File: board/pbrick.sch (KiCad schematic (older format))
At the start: 53 parts, among them J1 S8B-PH-SM4-TB_LF__SN_, J2 UJC-HP-3-SMT-TR, J3 QWIIC, J5 U.FL2PIN, J6 TC2030-IDC-NL, Q1 SSM6J507NU, Q2 SSM6J507NU, U1 TB67H420FTG(O,EL), U2 MIC5219-3.3YML-TR, U3 ADP3330ARTZ-5-RL7, U4 STUSB4500QTR

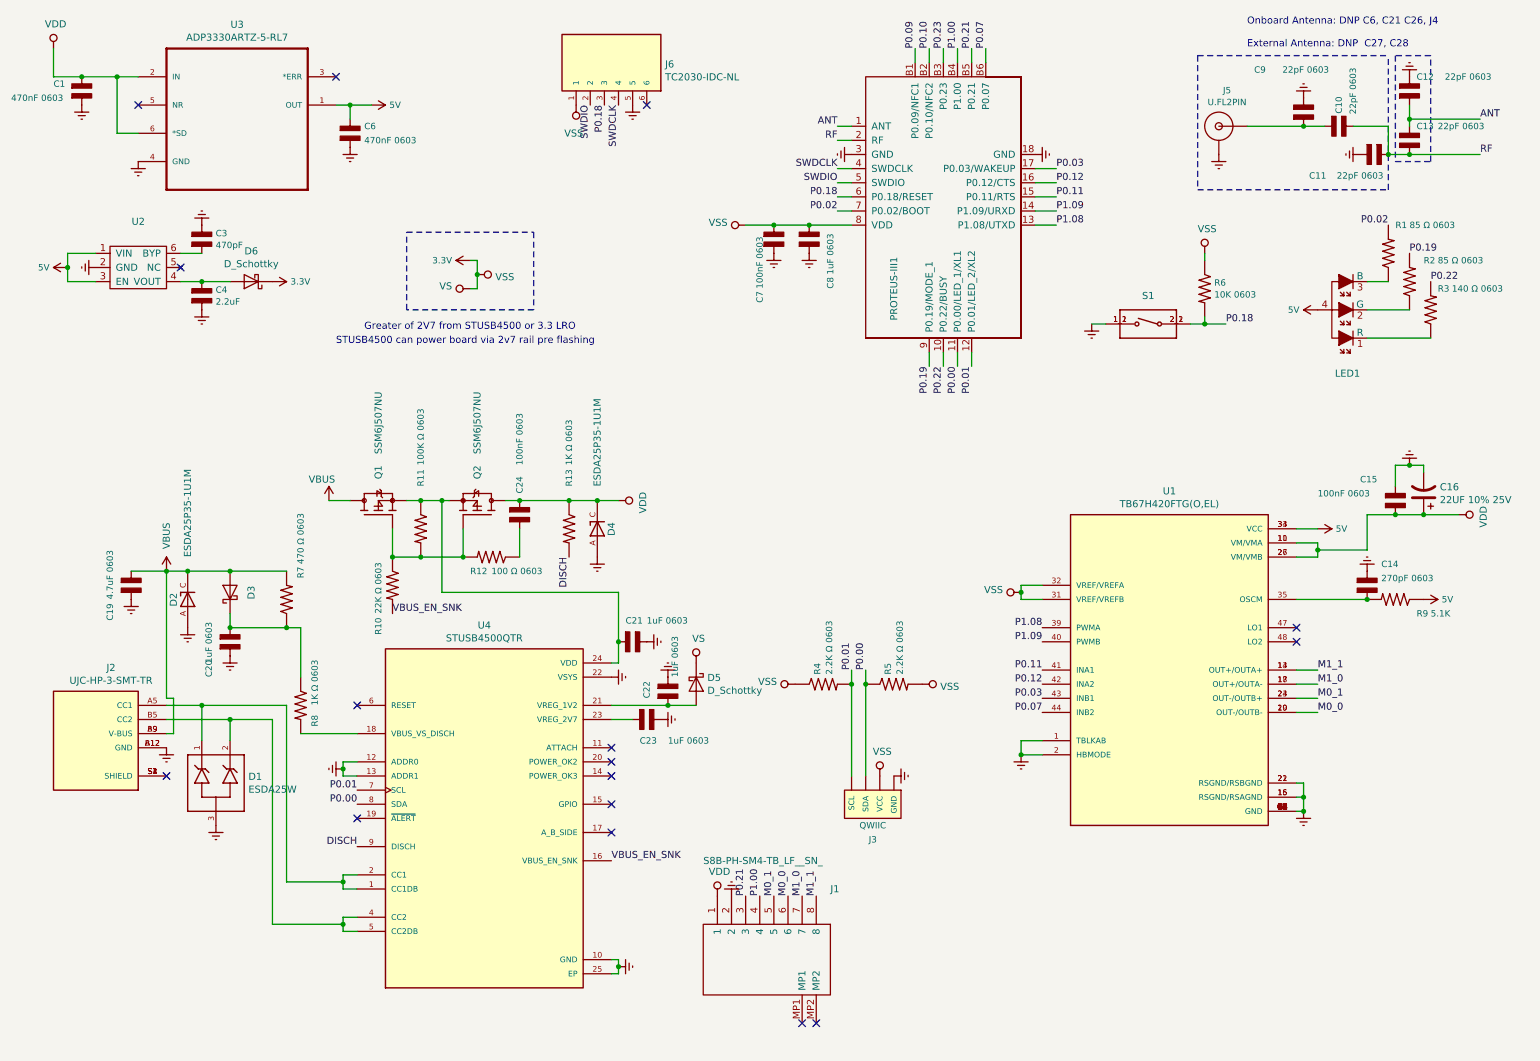
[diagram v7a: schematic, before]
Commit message: Starting work on STUSB4500 USB i2C connection for new board design
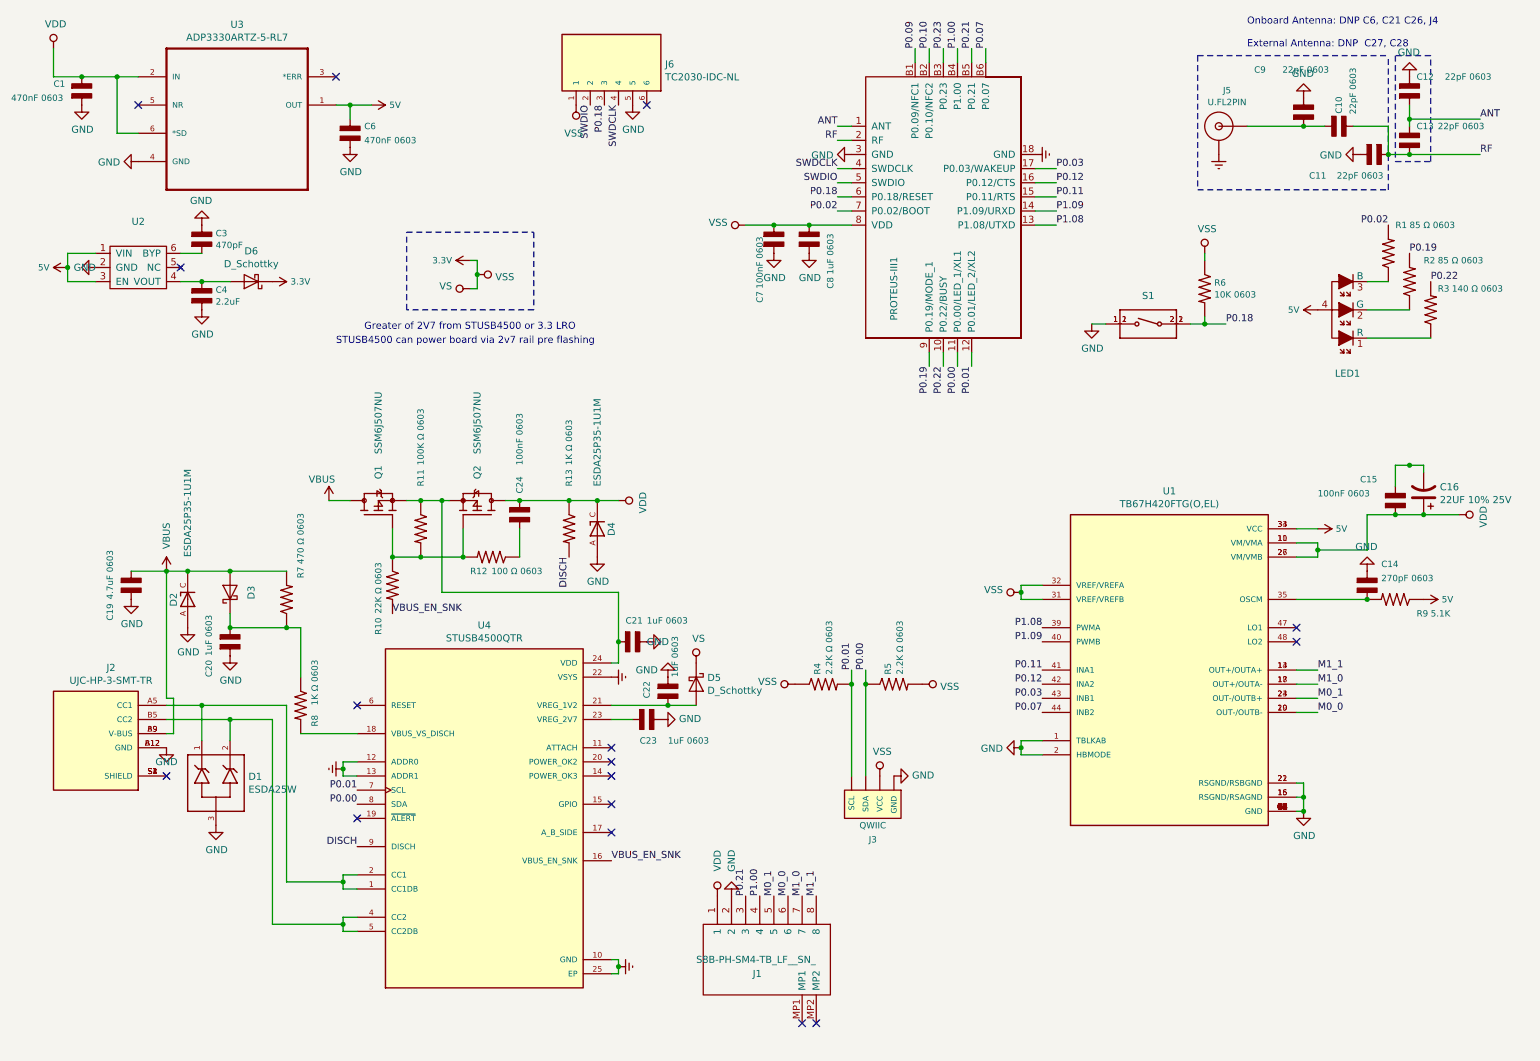
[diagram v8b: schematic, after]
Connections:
- net Earth: no longer C1.2, C11.2, C12.1, C14.1, C15.1, C16.2, C19.2, C20.2, C21.1, C22.1, C23.1, C3.1, C4.2, C6.2, C7.2, C8.2, C9.1, D1.3, D2.A, D4.A, J1.2, J2.A12 (GND), J2.B12 (GND), J3.1 (GND), J6.5, PROTEUS-III1.3 (GND), S1.1_1 (1), S1.1_2 (1), U1.1 (TBLKAB), U1.15 (RSGND/RSAGND), U1.16 (RSGND/RSAGND), U1.2 (HBMODE), U1.21 (RSGND/RSBGND), U1.22 (RSGND/RSBGND), U1.29 (GND), U1.30 (GND), U1.49 (GND), U1.50 (GND), U1.51 (GND), U1.52 (GND), U1.53 (GND), U1.54 (GND), U1.55 (GND), U1.56 (GND), U1.57 (GND), U1.58 (GND), U1.59 (GND), U1.60 (GND), U1.61 (GND), U1.62 (GND), U1.63 (GND), U1.64 (GND), U1.65 (GND), U1.66 (GND), U1.67 (GND), U1.68 (GND), U1.69 (GND), U1.70 (GND), U1.71 (GND), U1.72 (GND), U1.73 (GND), U1.74 (GND), U1.75 (GND), U1.76 (GND), U1.77 (GND), U1.78 (GND), U1.79 (GND), U1.8 (GND), U1.80 (GND), U1.81 (GND), U1.82 (GND), U1.83 (GND), U1.84 (GND), U1.85 (GND), U1.86 (GND), U1.87 (GND), U1.88 (GND), U1.89 (GND), U1.90 (GND), U1.91 (GND), U1.92 (GND), U1.93 (GND), U1.94 (GND), U1.95 (GND), U1.96 (GND), U1.97 (GND), U1.98 (GND), U1.G1 (GND), U1.G2 (GND), U1.G3 (GND), U1.G4 (GND), U2.2 (GND), U3.4 (GND)
- new net: C15.1, C16.2
- new net GND: C1.2, C11.2, C12.1, C14.1, C19.2, C20.2, C21.1, C22.1, C23.1, C3.1, C4.2, C6.2, C7.2, C8.2, C9.1, D1.3, D2.A, D4.A, J1.2, J2.A12 (GND), J2.B12 (GND), J3.1 (GND), J6.5, PROTEUS-III1.3 (GND), S1.1_1 (1), S1.1_2 (1), U1.1 (TBLKAB), U1.15 (RSGND/RSAGND), U1.16 (RSGND/RSAGND), U1.2 (HBMODE), U1.21 (RSGND/RSBGND), U1.22 (RSGND/RSBGND), U1.29 (GND), U1.30 (GND), U1.49 (GND), U1.50 (GND), U1.51 (GND), U1.52 (GND), U1.53 (GND), U1.54 (GND), U1.55 (GND), U1.56 (GND), U1.57 (GND), U1.58 (GND), U1.59 (GND), U1.60 (GND), U1.61 (GND), U1.62 (GND), U1.63 (GND), U1.64 (GND), U1.65 (GND), U1.66 (GND), U1.67 (GND), U1.68 (GND), U1.69 (GND), U1.70 (GND), U1.71 (GND), U1.72 (GND), U1.73 (GND), U1.74 (GND), U1.75 (GND), U1.76 (GND), U1.77 (GND), U1.78 (GND), U1.79 (GND), U1.8 (GND), U1.80 (GND), U1.81 (GND), U1.82 (GND), U1.83 (GND), U1.84 (GND), U1.85 (GND), U1.86 (GND), U1.87 (GND), U1.88 (GND), U1.89 (GND), U1.90 (GND), U1.91 (GND), U1.92 (GND), U1.93 (GND), U1.94 (GND), U1.95 (GND), U1.96 (GND), U1.97 (GND), U1.98 (GND), U1.G1 (GND), U1.G2 (GND), U1.G3 (GND), U1.G4 (GND), U2.2 (GND), U3.4 (GND)
